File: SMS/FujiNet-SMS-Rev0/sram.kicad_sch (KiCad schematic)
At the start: 5 parts, among them U2 AS6C4008-55TIN, U3 AS6C4008-55TIN

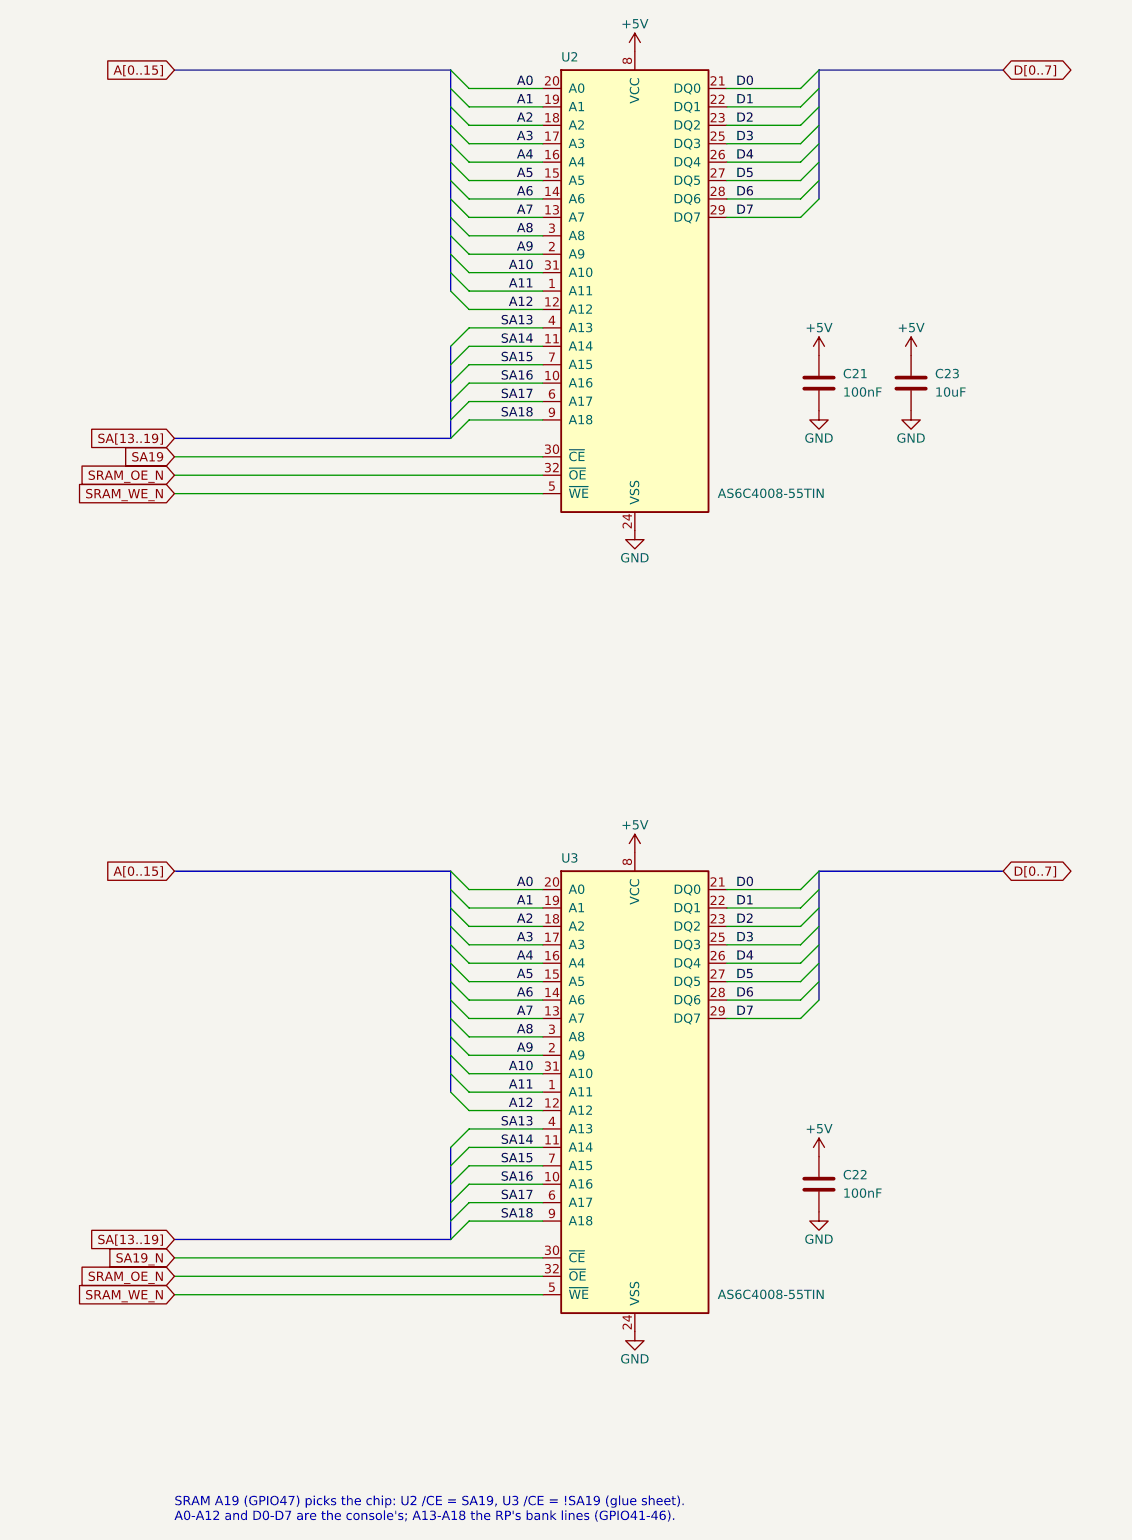
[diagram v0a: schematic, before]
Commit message: SMS Rev0: audit with kicad-happy + datasheets, fix the edge, redraw the schematic
Edge connector: every source (SMS Power slot diagram, little-scale, a 171-5519
scan, raphnet, the barbeque and reidrac footprints) puts the EVEN pins on the
component / label side with pins 1/2 at the right.  The schematic-only
footprint had the faces swapped, which would have put console +5V on /WR.
make_edge_fp.py now writes even pads on F.Cu, odd on B.Cu, 1.75 x 8.75 mm
fingers 0.75-9.5 mm from the edge on a 65.8 mm tab; check_nets.py asserts it
and tools/audit/edge_orientation.py checks it against the sources.

kicad-happy + datasheet audit (docs/design-review-rev0.md Part 1, 27 deep
review findings, gate 27/27): R_VBPD 4.7k VBUS pull-down (SS34 leakage lifts
the P-FET gate), /WAIT gate pull-up 10k -> 4.7k (GPIO34's reset pull-down vs
the 2N7002's 2.5 V threshold), 10 uF bulk on the console 5V.

Schematic: hierarchical sheets wired on a root block diagram (edge -> RP2354B
-> ESP32-S3 -> USB, glue and SRAM under the RP, power below); every sheet
drawn left to right, the glue as a wired logic network by gate depth, the
RP2354B mirrored so its bus faces the console, small sheets on A4.  Parts
are addressed by key (design.py), no more NES reference aliasing.  sch_draw
gains hierarchical labels, sheet blocks, a bus graph and flag / power-pin
lints; gen_sch checks the hierarchy against design.py and names nets by
their last path element (one bus vector per bus: KiCad joins differing
vectors by position).  ERC 0, check_nets 437/437, check_glue 8192/8192.

JLC CPL rotations measured against the EasyEDA footprint of every LCSC part
(tools/audit/jlc); the AS6C4008 has no EasyEDA footprint.

Co-Authored-By: Claude Opus 5.5 <noreply@anthropic.com>
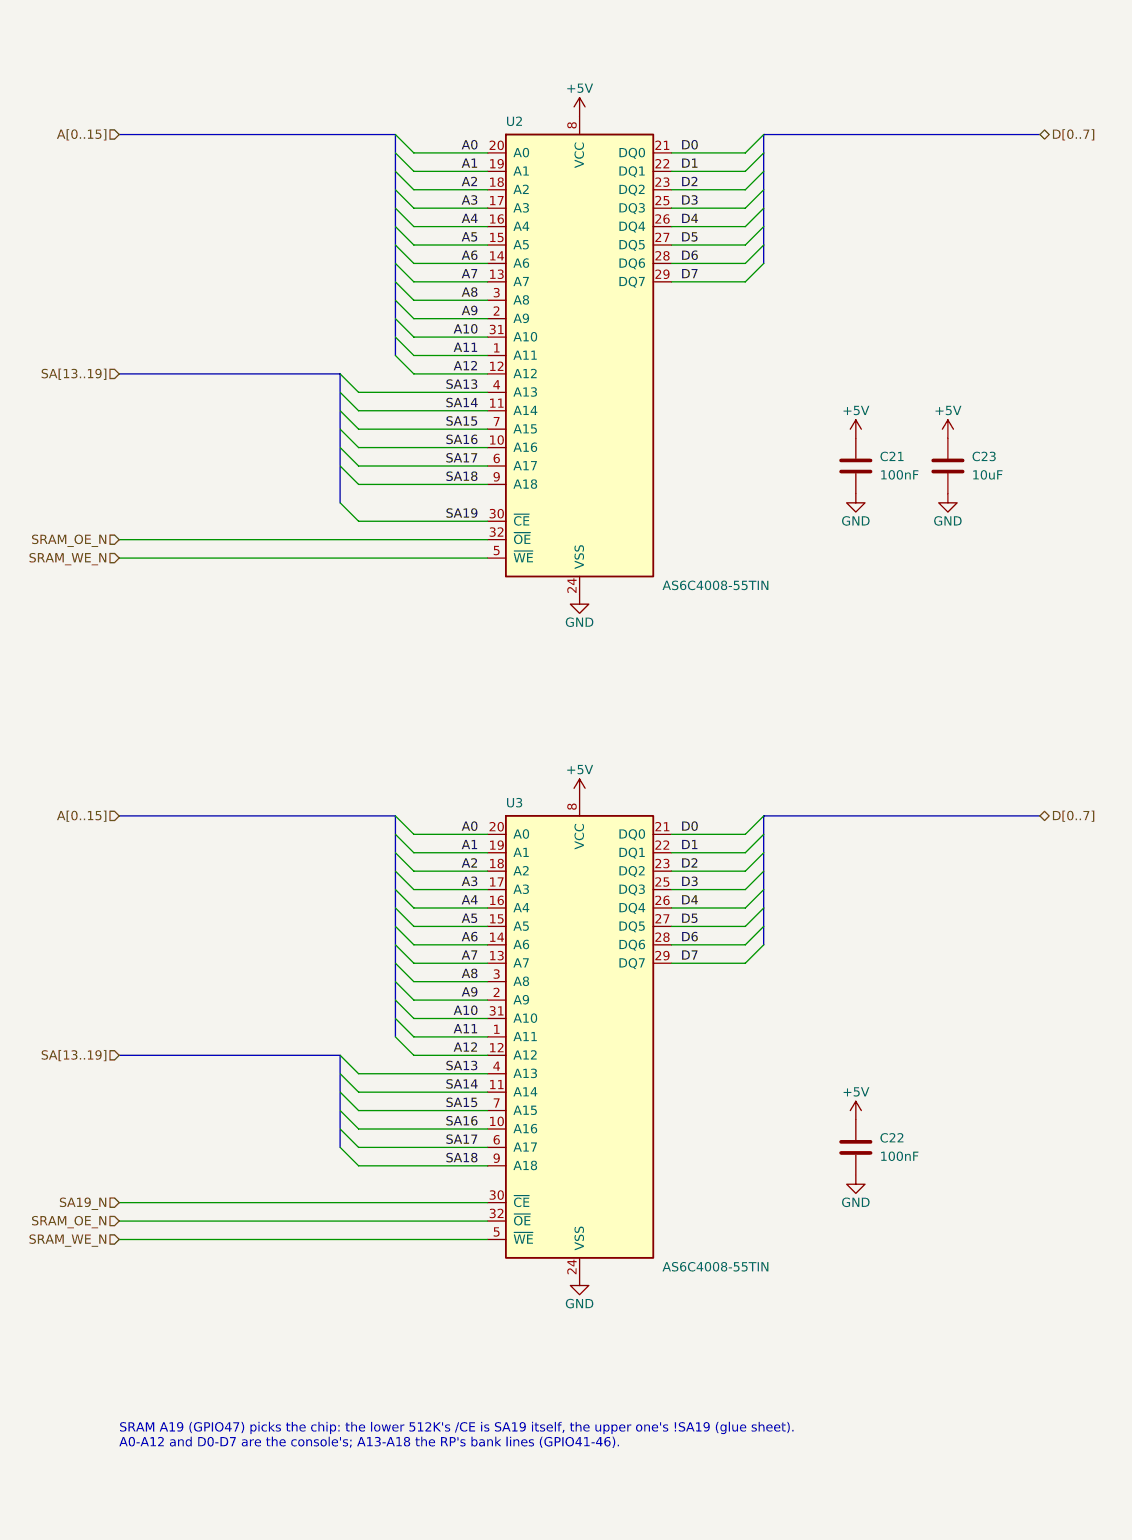
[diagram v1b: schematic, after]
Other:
- note added: "SRAM A19 (GPIO47) picks the chip: the lower 512K's /CE is SA19 itself, the upper one's !SA19 (glue sheet). A0-A12 and D0-D7 are the console's; A13-A18 the RP's bank lines (GPIO41-46)."
- note removed: "SRAM A19 (GPIO47) picks the chip: U2 /CE = SA19, U3 /CE = !SA19 (glue sheet). A0-A12 and D0-D7 are the console's; A13-A18 the RP's bank lines (GPIO41-46)."
- moved on the sheet: C21, C22, C23, U2, U3

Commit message: SMS Rev0 v2: port the FujiNet-7800 tooling, swap the near-stock-out parts
- export.py: JLCPCB and PCBWay packages (PCBWay turnkey BOM, centroid,
  assembly drawing); Manufacturer on every BOM part (design.MFR), written
  to symbols and footprints alike
- edge_geom.py: the SMS edge constants in one place (make_edge_fp,
  gen_pcb, check_gerbers); gen_pcb's body height, holes and In4 split now
  come from placement.py
- footprint paths from the schematic netlist (gen_pcb.fp_sheet_unit), so
  a part's units can be drawn on several sheets (prototype 2026-10-08:
  kicad-cli files it under the first sheet, parity accepts it)
- check_vias, check_gerbers, make_happy_config, stitch_gnd second ring,
  set_models main(), route_board.sh 12 passes / hybrid, DRC at all
  severities
- TL3342 -> TS-1187A-B-A-B (C318884), WS2812B-2020-V6 -> WS2812C-2020-V1
  (C2976072): ~5 in stock on 2026-10-07

Co-Authored-By: Claude Opus 5.5 <noreply@anthropic.com>
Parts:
- C21, C22: Manufacturer (none) -> YAGEO
- C23: Manufacturer (none) -> Samsung Electro-Mechanics
- U2, U3: Manufacturer (none) -> Alliance Memory
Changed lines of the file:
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@@
+			)
+		)
+		(property "Manufacturer" "Alliance Memory"
+			(at 210.82 76.2 0)
+			(effects
+				(font
+					(size 1.27 1.27)
+				)
+				(hide yes)
 			)
 		)
@@
 			)
 		)
+		(property "Manufacturer" "YAGEO"
+			(at 248.92 91.44 0)
+			(effects
+				(font
+					(size 1.27 1.27)
+				)
+				(hide yes)
+			)
+		)
 		(property "LCSC" "C14663"
 			(at 248.92 91.44 0)
@@
 			)
 		)
+		(property "Manufacturer" "Samsung Electro-Mechanics"
+			(at 261.62 91.44 0)
+			(effects
+				(font
+					(size 1.27 1.27)
+				)
+				(hide yes)
+			)
+		)
 		(property "LCSC" "C19702"
 			(at 261.62 91.44 0)
@@
 			)
 		)
+		(property "Manufacturer" "Alliance Memory"
+			(at 210.82 170.18 0)
+			(effects
+				(font
+					(size 1.27 1.27)
+				)
+				(hide yes)
+			)
+		)
 		(property "LCSC" "C5569980"
 			(at 210.82 170.18 0)
@@
 			(at 248.92 185.42 0)
 			(effects
+				(font
+					(size 1.27 1.27)
+				)
+				(hide yes)
+			)
+		)
+		(property "Manufacturer" "YAGEO"
+			(at 248.92 185.42 0)
+			(effects
